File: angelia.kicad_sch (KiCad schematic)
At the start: 207 parts, among them J10 Conn_Coaxial, J15 Conn_02x05_Top_Bottom, J16 Conn_02x13_Top_Bottom, J18 Conn_02x05_Top_Bottom, J25 Conn_Coaxial, J3 Conn_Coaxial, J5 Conn_Coaxial, P1 Conn_02x05_Top_Bottom, P2 Conn_02x05_Top_Bottom, U10 LTC2208xUP, U18 LTC2208xUP, U5 EP4CE115F780

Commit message: beginning special components
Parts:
- removed D1: D_Small, symbol Device:D_Small
- removed R1: R_Small, Resistor_SMD:R_0805_2012Metric, symbol Device:R_Small
- added C103, C107, C170, C172, C179, C180, C239, C242, C251, C70, C72, C73: 1n, Capacitor_SMD:C_0805_2012Metric, symbol Device:C_Small
- added C105, C173, C175, C206, C75, C87: 100p, Capacitor_SMD:C_0805_2012Metric, symbol Device:C_Small
- added C121, C130, C131, C136, C140, C42, C59, C82: 10n, Capacitor_SMD:C_0402_1005Metric, symbol Device:C_Small
- added C165, C176, C178, C181, C184, C186, C195: 10u, Capacitor_SMD:C_0805_2012Metric, symbol Device:C_Small
- added D10, D11, D12, D13, D14, D15, D16, D17, D18, D19: LED_Small, LED_SMD:LED_0805_2012Metric, symbol Device:LED_Small
- added F1, F2, F3, F4, F5: Fuse_Small, Fuse_smd:Fuse_1812_4532Metric, symbol Device:Fuse_Small
- added J7: RJ45, Connector_RJ:RJ45_Amphenol_54602-x08_Horizontal, symbol Connector:RJ45
- added L26, L29, L31, L35, L36, L37, L39: FerriteBead_Small, Ferrite_LC_NFM41P:Ferrite_LC_NFM41P, symbol Device:FerriteBead_Small
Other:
- moved on the sheet: C1, C10, C100, C101, C102, C104, C106, C108, C109, C11, C110, C111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

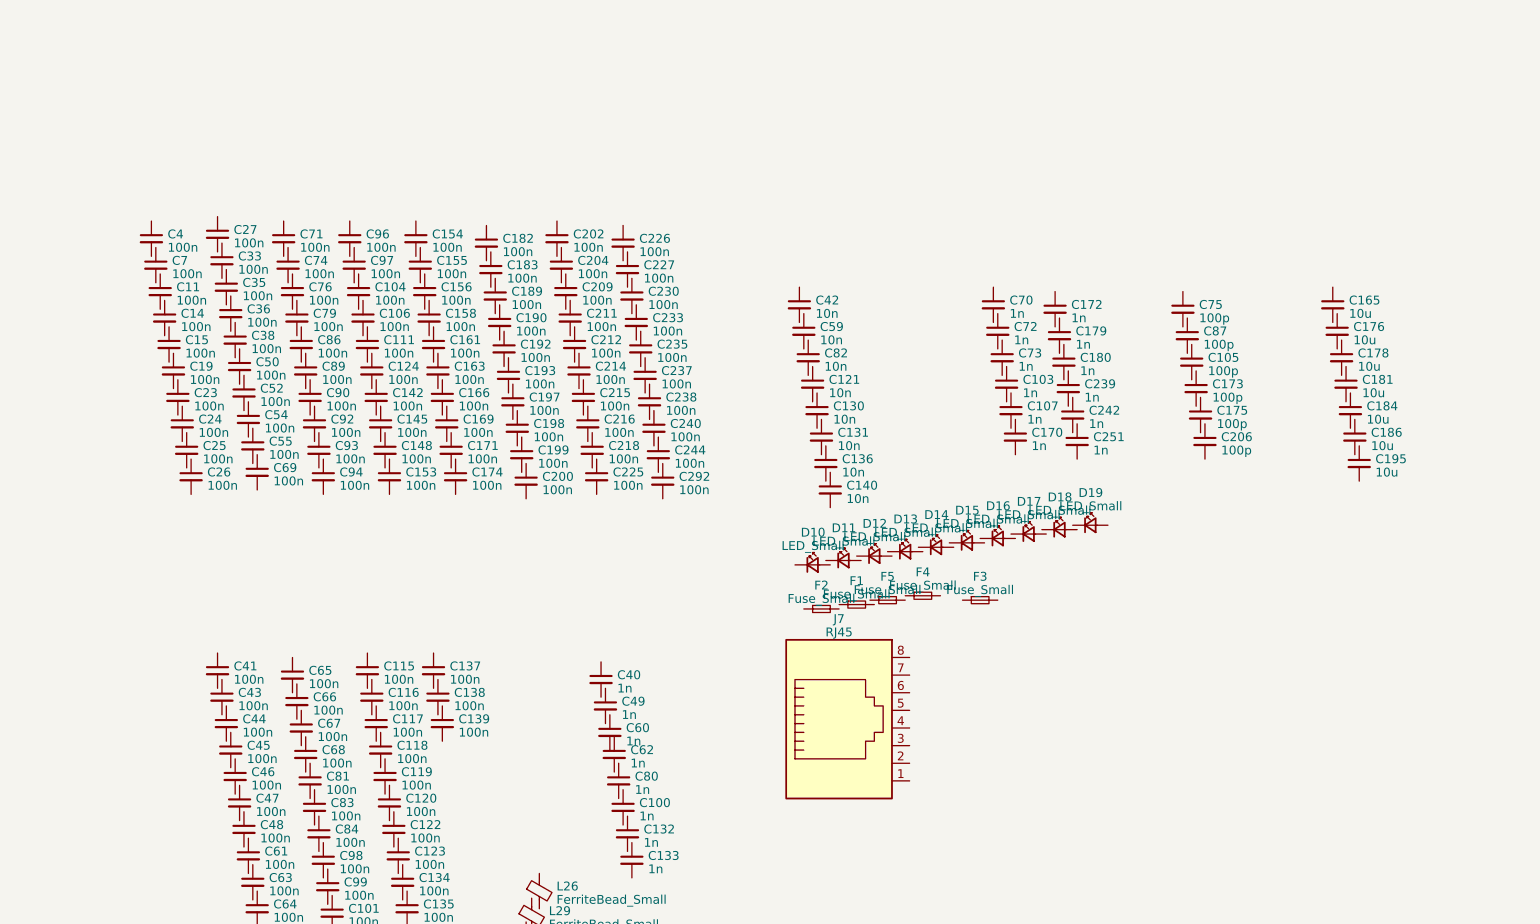
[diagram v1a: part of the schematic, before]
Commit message: some more caps, still some more caps and RJ45
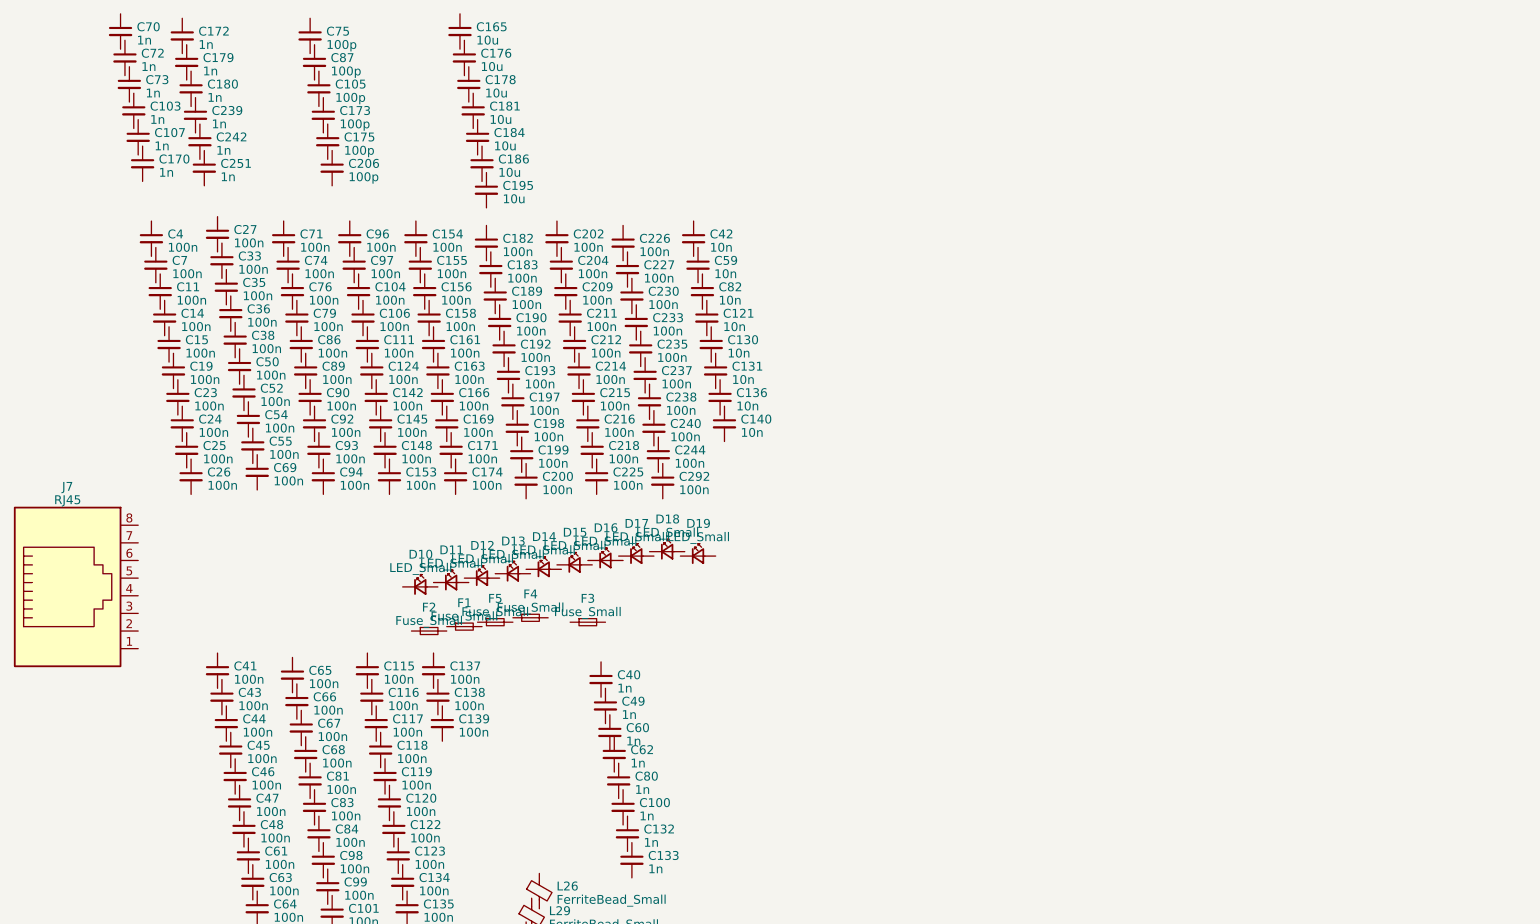
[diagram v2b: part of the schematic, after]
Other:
- moved on the sheet: C103, C105, C107, C121, C130, C131, C136, C140, C165, C170, C172, C173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

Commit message: ferrites and vlsi
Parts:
- added J33: ATX-20, Connector_Molex:Molex_Mini-Fit_Jr_5566-20A_2x10_P4.20mm_Vertical, symbol Connector:ATX-20
- added L1, L10, L11, L12, L14, L15, L16, L2, L20, L21, L22, L23, L24, L30, L32, L33, L38, L41, L42, L43, L44, L45, L6, L8, L9: 220, Inductor_SMD:L_0805_2012Metric_Pad1.05x1.20mm_HandSolder, symbol Device:L
- added L3: 560nH, Inductor_SMD:L_0805_2012Metric_Pad1.05x1.20mm_HandSolder, symbol Device:L
- added L4: 22n, Inductor_SMD:L_0805_2012Metric_Pad1.05x1.20mm_HandSolder, symbol Device:L
- added U14: SN65LVDM180D, Package_SO:SOIC-14_3.9x8.7mm_P1.27mm, symbol Analog_ADC:MCP3428
- added U22: ULN2003A, Package_SO:SOIC-16W_5.3x10.2mm_P1.27mm, symbol Transistor_Array:ULN2003A
- added U3, U4: LMC6482AM, Package_SO:SO-8_5.3x6.2mm_P1.27mm, symbol Regulator_Linear:LP2951-3.0_SOIC
- added U301: ~, Package_SO:TSOP-I-48_18.4x12mm_P0.5mm, symbol cy_memory:CY62177EV30LL
- added U6, U7: OPA2674IC, Package_SO:SO-8_5.3x6.2mm_P1.27mm, symbol Regulator_Linear:LP2951-3.0_SOIC
- renumbered U5 to P3
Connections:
- new net: J33.1 (+3.3V), J33.11 (+3.3V), J33.2 (+3.3V)
- new net: J33.13 (GND), J33.15 (GND), J33.16 (GND), J33.17 (GND), J33.3 (GND), J33.5 (GND), J33.7 (GND)
- new net: J33.19 (+5V), J33.20 (+5V), J33.4 (+5V), J33.6 (+5V)
- new net: U301., U301.63

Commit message: ferrites and lna
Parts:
- added U11, U23: LTC6400, Package_DFN_QFN:QFN-16-1EP_3x3mm_P0.5mm_EP1.7x1.7mm_ThermalVias, symbol Amplifier_Operational:LTC1152
- added U19, U31: TO-252-5, Package_TO_SOT_SMD:TO-252-5_TabPin3, symbol Regulator_Linear:LP38512TS-1.8
- added U27: TO-252-3, Package_TO_SOT_SMD:TO-252-3_TabPin2, symbol Regulator_Linear:LP38512TS-1.8
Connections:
- new net: U19.3 (GND), U19.6 (GND)
- new net: U31.3 (GND), U31.6 (GND)
- new net: U27.3 (GND), U27.6 (GND)
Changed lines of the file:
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@@
     )
   )
+  (symbol (lib_id "Regulator_Linear:LP38512TS-1.8") (at 26.035 153.035 0) (unit 1)
+    (in_bom yes) (on_board yes) (dnp no) (fields_autoplaced)
+    (property "Reference" "U19" (at 26.035 145.5801 0)
+      (effects (font (size 1.27 1.27)))
+    )
+    (property "Value" "TO-252-5" (at 26.035 147.5011 0)
+      (effects (font (size 1.27 1.27)))
+    )
+    (property "Footprint" "Package_TO_SOT_SMD:TO-252-5_TabPin3" (at 26.035 153.035 0)
+      (effects (font (size 1.27 1.27)) hide)
+    )
+    (property "Datasheet" "http://www.ti.com/lit/ds/symlink/lp38512.pdf" (at 26.035 153.035 0)
+      (effects (font (size 1.27 1.27)) hide)
+    )
+    (pin "1")
+    (pin "2")
+    (pin "3")
+    (pin "4")
+    (pin "5")
+    (pin "6")
+    (instances
+      (project "angelia"
+        (path "/2b733a3a-238e-4552-84a8-ec9891c3916f"
+          (reference "U19") (unit 1)
+        )
+      )
+    )
+  )
   (symbol (lib_id "Device:C_Small") (at -53.975 95.885 0) (unit 1)
     (in_bom yes) (on_board yes) (dnp no) (fields_autoplaced)
@@
     )
   )
+  (symbol (lib_id "Regulator_Linear:LP38512TS-1.8") (at 48.26 153.67 0) (unit 1)
+    (in_bom yes) (on_board yes) (dnp no) (fields_autoplaced)
+    (property "Reference" "U31" (at 48.26 146.2151 0)
+      (effects (font (size 1.27 1.27)))
+    )
+    (property "Value" "TO-252-5" (at 48.26 148.1361 0)
+      (effects (font (size 1.27 1.27)))
+    )
+    (property "Footprint" "Package_TO_SOT_SMD:TO-252-5_TabPin3" (at 48.26 153.67 0)
+      (effects (font (size 1.27 1.27)) hide)
+    )
+    (property "Datasheet" "http://www.ti.com/lit/ds/symlink/lp38512.pdf" (at 48.26 153.67 0)
+      (effects (font (size 1.27 1.27)) hide)
+    )
+    (pin "1")
+    (pin "2")
+    (pin "3")
+    (pin "4")
+    (pin "5")
+    (pin "6")
+    (instances
+      (project "angelia"
+        (path "/2b733a3a-238e-4552-84a8-ec9891c3916f"
+          (reference "U31") (unit 1)
+        )
+      )
+    )
+  )
   (symbol (lib_id "Device:C_Polarized_Small") (at 356.235 69.215 0) (unit 1)
     (in_bom yes) (on_board yes) (dnp no) (fields_autoplaced)
@@
     )
   )
+  (symbol (lib_id "Amplifier_Operational:LTC1152") (at 308.61 109.855 0) (unit 1)
+    (in_bom yes) (on_board yes) (dnp no) (fields_autoplaced)
+    (property "Reference" "U11" (at 318.5753 106.7181 0)
+      (effects (font (size 1.27 1.27)))
+    )
+    (property "Value" "LTC6400" (at 318.5753 108.6391 0)
+      (effects (font (size 1.27 1.27)))
+    )
+    (property "Footprint" "Package_DFN_QFN:QFN-16-1EP_3x3mm_P0.5mm_EP1.7x1.7mm_ThermalVias" (at 288.29 100.965 0)
+      (effects (font (size 1.27 1.27)) hide)
+    )
+    (property "Datasheet" "https://www.analog.com/media/en/technical-documentation/data-sheets/lt1152.pdf" (at 288.29 100.965 0)
+      (effects (font (size 1.27 1.27)) hide)
+    )
+    (pin "1")
+    (pin "2")
+    (pin "3")
+    (pin "4")
+    (pin "5")
+    (pin "6")
+    (pin "7")
+    (pin "8")
+    (instances
+      (project "angelia"
+        (path "/2b733a3a-238e-4552-84a8-ec9891c3916f"
+          (reference "U11") (unit 1)
+        )
+      )
+    )
+  )
   (symbol (lib_id "Device:C_Small") (at 1.905 21.59 0) (unit 1)
     (in_bom yes) (on_board yes) (dnp no) (fields_autoplaced)
@@
     )
   )
+  (symbol (lib_id "Amplifier_Operational:LTC1152") (at 334.01 110.49 0) (unit 1)
+    (in_bom yes) (on_board yes) (dnp no) (fields_autoplaced)
+    (property "Reference" "U23" (at 343.9753 107.3531 0)
+      (effects (font (size 1.27 1.27)))
+    )
+    (property "Value" "LTC6400" (at 343.9753 109.2741 0)
+      (effects (font (size 1.27 1.27)))
+    )
+    (property "Footprint" "Package_DFN_QFN:QFN-16-1EP_3x3mm_P0.5mm_EP1.7x1.7mm_ThermalVias" (at 313.69 101.6 0)
+      (effects (font (size 1.27 1.27)) hide)
+    )
+    (property "Datasheet" "https://www.analog.com/media/en/technical-documentation/data-sheets/lt1152.pdf" (at 313.69 101.6 0)
+      (effects (font (size 1.27 1.27)) hide)
+    )
+    (pin "1")
+    (pin "2")
+    (pin "3")
+    (pin "4")
+    (pin "5")
+    (pin "6")
+    (pin "7")
+    (pin "8")
+    (instances
+      (project "angelia"
+        (path "/2b733a3a-238e-4552-84a8-ec9891c3916f"
+          (reference "U23") (unit 1)
+        )
+      )
+    )
+  )
   (symbol (lib_id "Device:C_Polarized_Small") (at 356.87 73.025 0) (mirror x) (unit 1)
     (in_bom yes) (on_board yes) (dnp no)
@@
         )
       )
+    )
+  )
+  (symbol (lib_id "Regulator_Linear:LP38512TS-1.8") (at 22.86 170.815 0) (unit 1)
+    (in_bom yes) (on_board yes) (dnp no) (fields_autoplaced)
+    (property "Reference" "U27" (at 22.86 163.3601 0)
+      (effects (font (size 1.27 1.27)))
+    )
+    (property "Value" "TO-252-3" (at 22.86 165.2811 0)
+      (effects (font (size 1.27 1.27)))
+    )
+    (property "Footprint" "Package_TO_SOT_SMD:TO-252-3_TabPin2" (at 22.86 170.815 0)
+      (effects (font (size 1.27 1.27)) hide)
+    )
+    (property "Datasheet" "http://www.ti.com/lit/ds/symlink/lp38512.pdf" (at 22.86 170.815 0)
+      (effects (font (size 1.27 1.27)) hide)
+    )
+    (pin "1")
+    (pin "2")
+    (pin "3")
+    (pin "4")
+    (pin "5")
+    (pin "6")
+    (instances
+      (project "angelia"
+        (path "/2b733a3a-238e-4552-84a8-ec9891c3916f"
+          (reference "U27") (unit 1)
+        )
+      )

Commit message: more vlsi, more inductances
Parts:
- added FL10, FL11, FL12, FL14, FL15, FL16, FL17, FL18, FL19, FL2, FL21, FL3, FL4, FL5, FL7, FL8, FL9: AF, Inductor_SMD:L_1806_4516Metric, symbol Device:L
- added L13, L17, L18, L19: 47n, Inductor_SMD:L_0805_2012Metric_Pad1.05x1.20mm_HandSolder, symbol Device:L
- added U13: KSZ9021RL, Package_QFP:LQFP-64-1EP_10x10mm_P0.5mm_EP5x5mm, symbol Interface_Ethernet:KSZ9031RNXCA
- added U2: TLV320AIC23BPW, Package_SO:TSSOP-28_4.4x9.7mm_P0.65mm, symbol Audio:TLV320AIC23BPW
- added U20, U25: 74LCX541MTC, Package_SO:TSSOP-20_4.4x5mm_P0.5mm, symbol 74xx:74HC596
- added U5: AD9744, Package_SO:TSSOP-28_4.4x9.7mm_P0.65mm, symbol Analog_DAC:AD9744
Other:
- moved on the sheet: L1, L10, L11, L12, L14, L15, L16, L2, L20, L21, L22, L23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

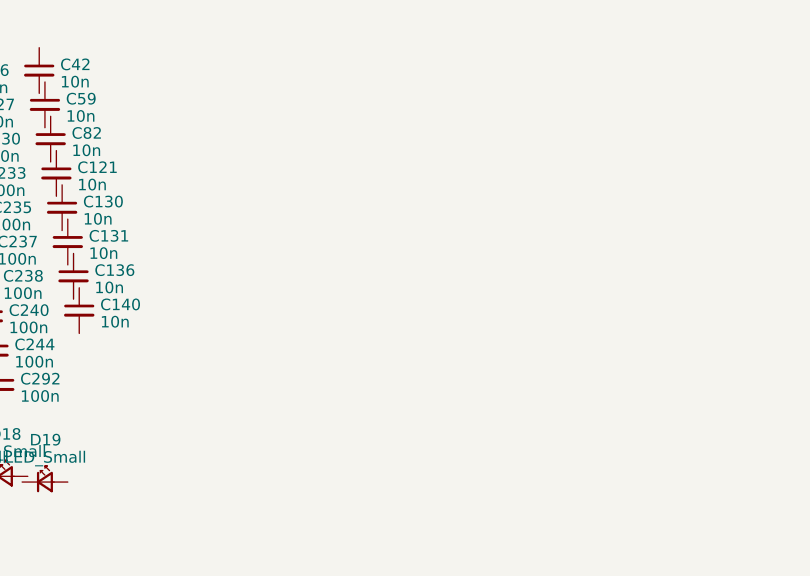
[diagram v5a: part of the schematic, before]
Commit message: all mlcc are done
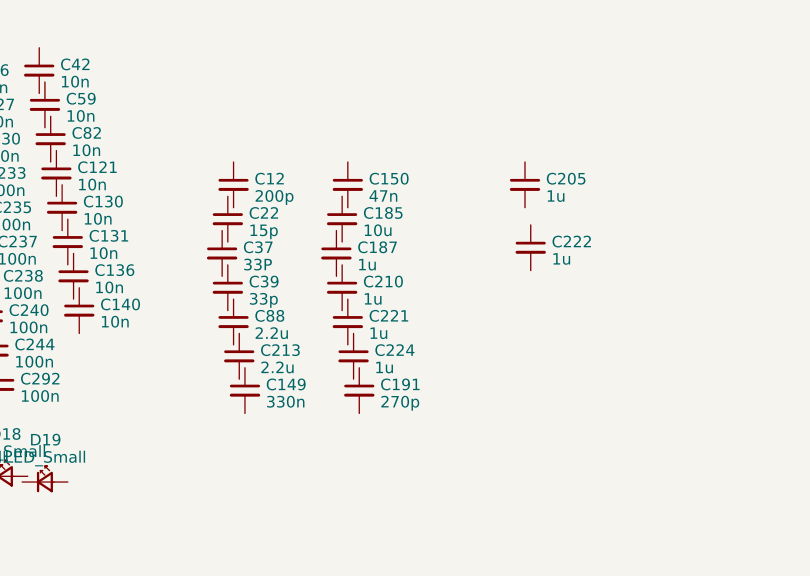
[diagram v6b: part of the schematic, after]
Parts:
- added C12: 200p, Capacitor_SMD:C_0805_2012Metric, symbol Device:C_Small
- added C149: 330n, Capacitor_SMD:C_0805_2012Metric, symbol Device:C_Small
- added C150: 47n, Capacitor_SMD:C_0805_2012Metric, symbol Device:C_Small
- added C185: 10u, Capacitor_SMD:C_0805_2012Metric, symbol Device:C_Small
- added C187, C210, C221, C224: 1u, Capacitor_SMD:C_0805_2012Metric, symbol Device:C_Small
- added C191: 270p, Capacitor_SMD:C_0805_2012Metric, symbol Device:C_Small
- added C205, C222: 1u, Capacitor_Tantalum_SMD:CP_EIA-3216-10_Kemet-I, symbol Device:C_Small
- added C213, C88: 2.2u, Capacitor_SMD:C_0805_2012Metric, symbol Device:C_Small
- added C22: 15p, Capacitor_SMD:C_0805_2012Metric, symbol Device:C_Small
- added C37: 33P, Capacitor_SMD:C_0805_2012Metric, symbol Device:C_Small
- added C39: 33p, Capacitor_SMD:C_0805_2012Metric, symbol Device:C_Small

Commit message: most pull-up resistor done
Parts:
- added R10, R106, R108, R111, R112, R113, R114, R116, R117, R122, R123, R124, R125, R136, R137, R2, R40, R41, R42, R50, R52, R53, R54, R58, R64, R65, R66, R67, R68, R69, R70, R71, R72, R75, R78, R82: 10k, Resistor_SMD:R_0805_2012Metric, symbol Device:R_Small
- added R103, R109, R120, R121, R130, R133, R16, R21, R26, R3, R43, R48, R49, R61, R79, R85: 1k, Resistor_SMD:R_0805_2012Metric, symbol Device:R_Small
- added R119, R131, R135, R47, R60, R77, R84, R86, R87: 0R, Resistor_SMD:R_0805_2012Metric, symbol Device:R_Small
- added R129, R138, R140, R20, R76: 3K3, Resistor_SMD:R_0805_2012Metric, symbol Device:R_Small
- added R132, R5, R6, R88, R89, R90, R91, R92, R93, R94, R95, R96, R97: 2.2k, Resistor_SMD:R_0805_2012Metric, symbol Device:R_Small
- added R25, R28, R29, R33, R34, R4: 22R, Resistor_SMD:R_0805_2012Metric, symbol Device:R_Small
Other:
- moved on the sheet: C12, C149, C150, C185, C187, C191, C205, C210, C213, C22, C221, C222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
